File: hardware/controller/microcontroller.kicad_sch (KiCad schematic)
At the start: 43 parts, among them J2 IDC-10, J3 USB_C_Receptacle_USB2.0_14P, SW1 SW_Push, SW2 SW_Push, SW3 SW_Push, U1 STM32U535RET6, U2 nRF24L01+ 2.4Gz Mini SMD, U3 ESP32-C3-WROOM-02, U4 SRV05-4, Y1 8MHz

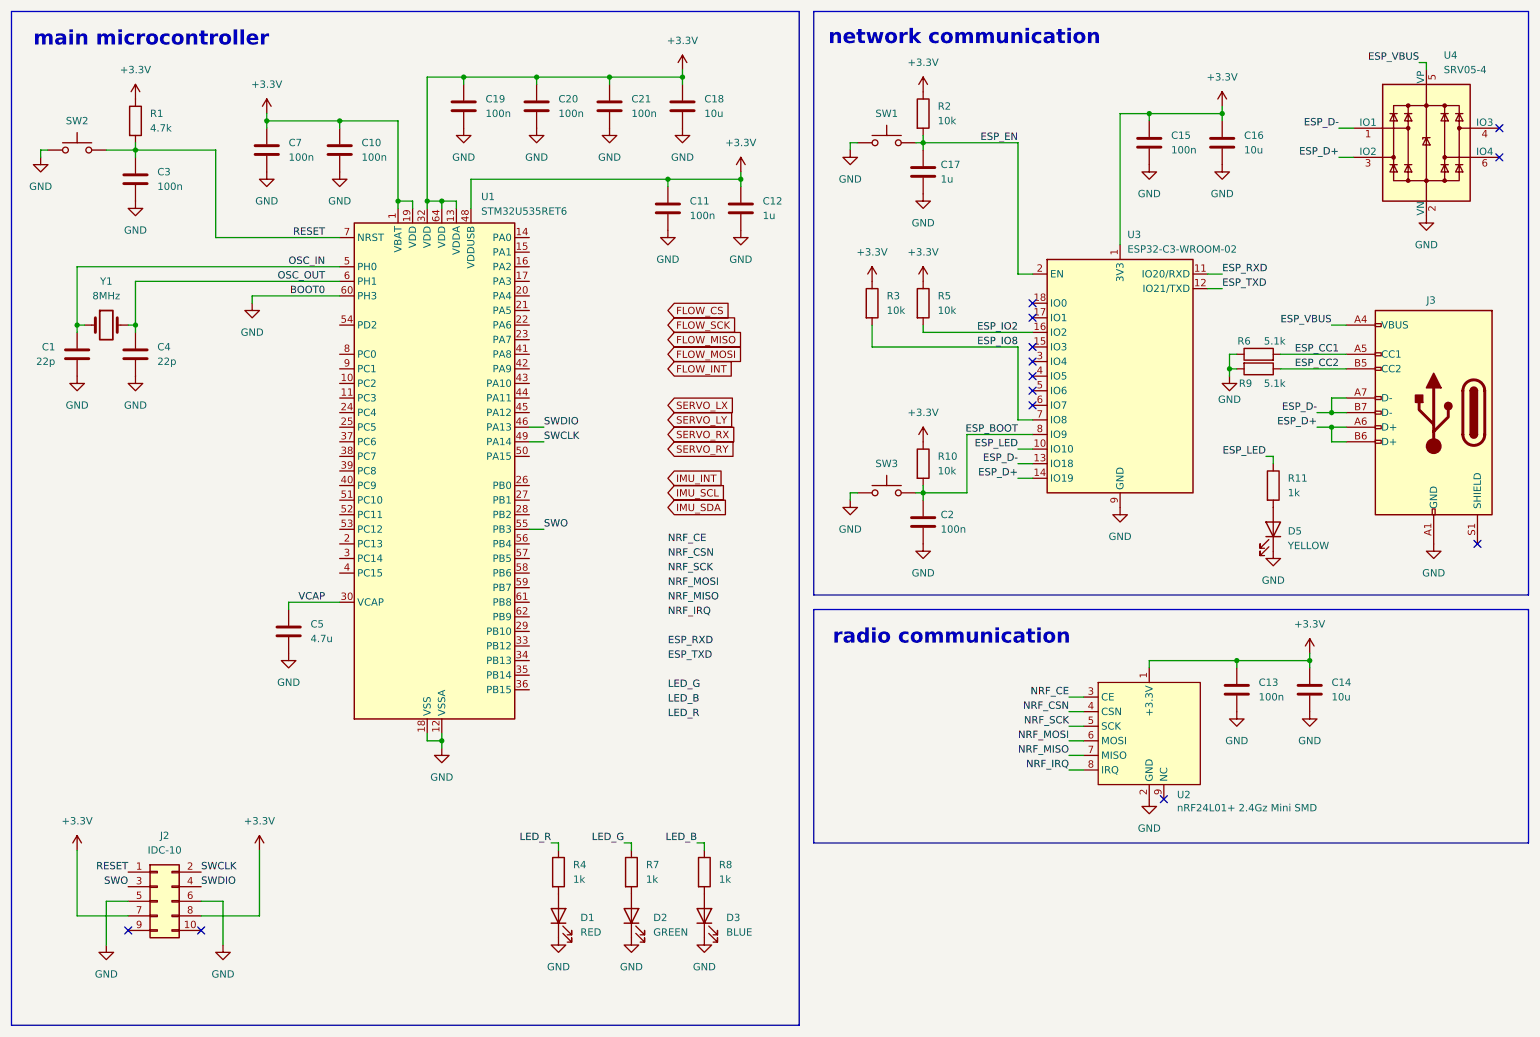
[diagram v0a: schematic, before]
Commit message: add IMU, FLOW, 5V, 3.3V, MOSFET SW
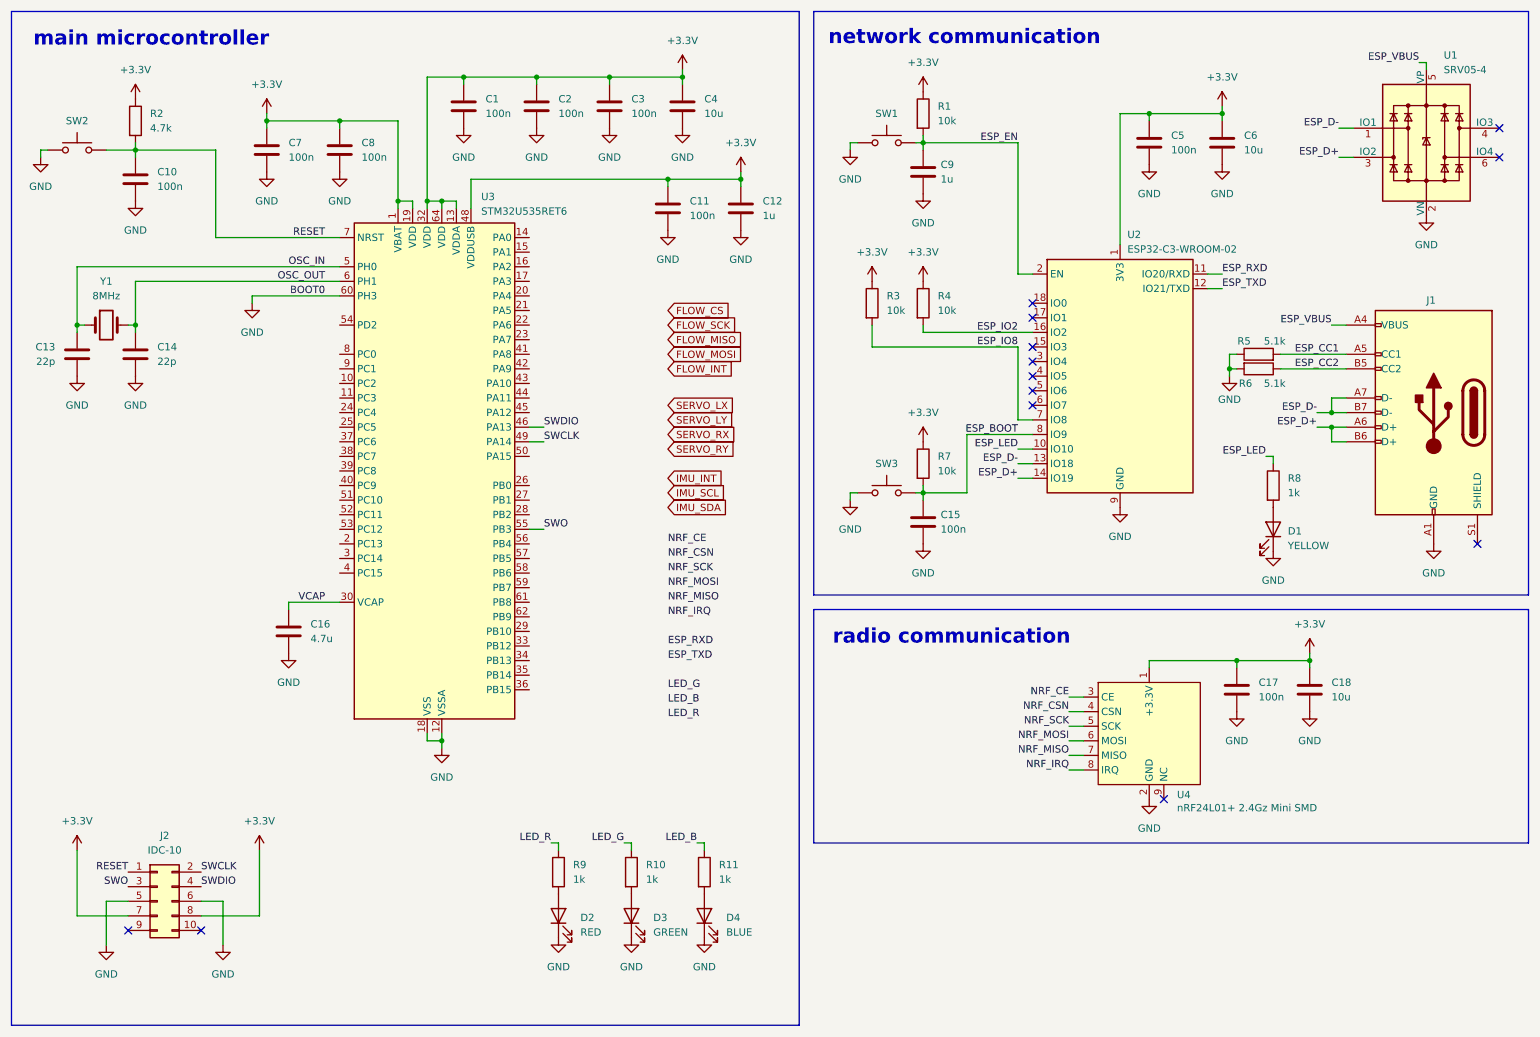
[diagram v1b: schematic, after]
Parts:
- renumbered C19 to C1, C3 to C10, C1 to C13, C4 to C14, C2 to C15, C5 to C16, C13 to C17, C14 to C18, C20 to C2, C21 to C3, C18 to C4, C15 to C5, C16 to C6, C10 to C8, C17 to C9, D5 to D1, D1 to D2, D2 to D3, D3 to D4, J3 to J1, R2 to R1, R7 to R10, R8 to R11, R1 to R2, R5 to R4, R6 to R5, R9 to R6, R10 to R7, R11 to R8, R4 to R9, U4 to U1, U3 to U2, U1 to U3, U2 to U4

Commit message: uC pinout and second power stage
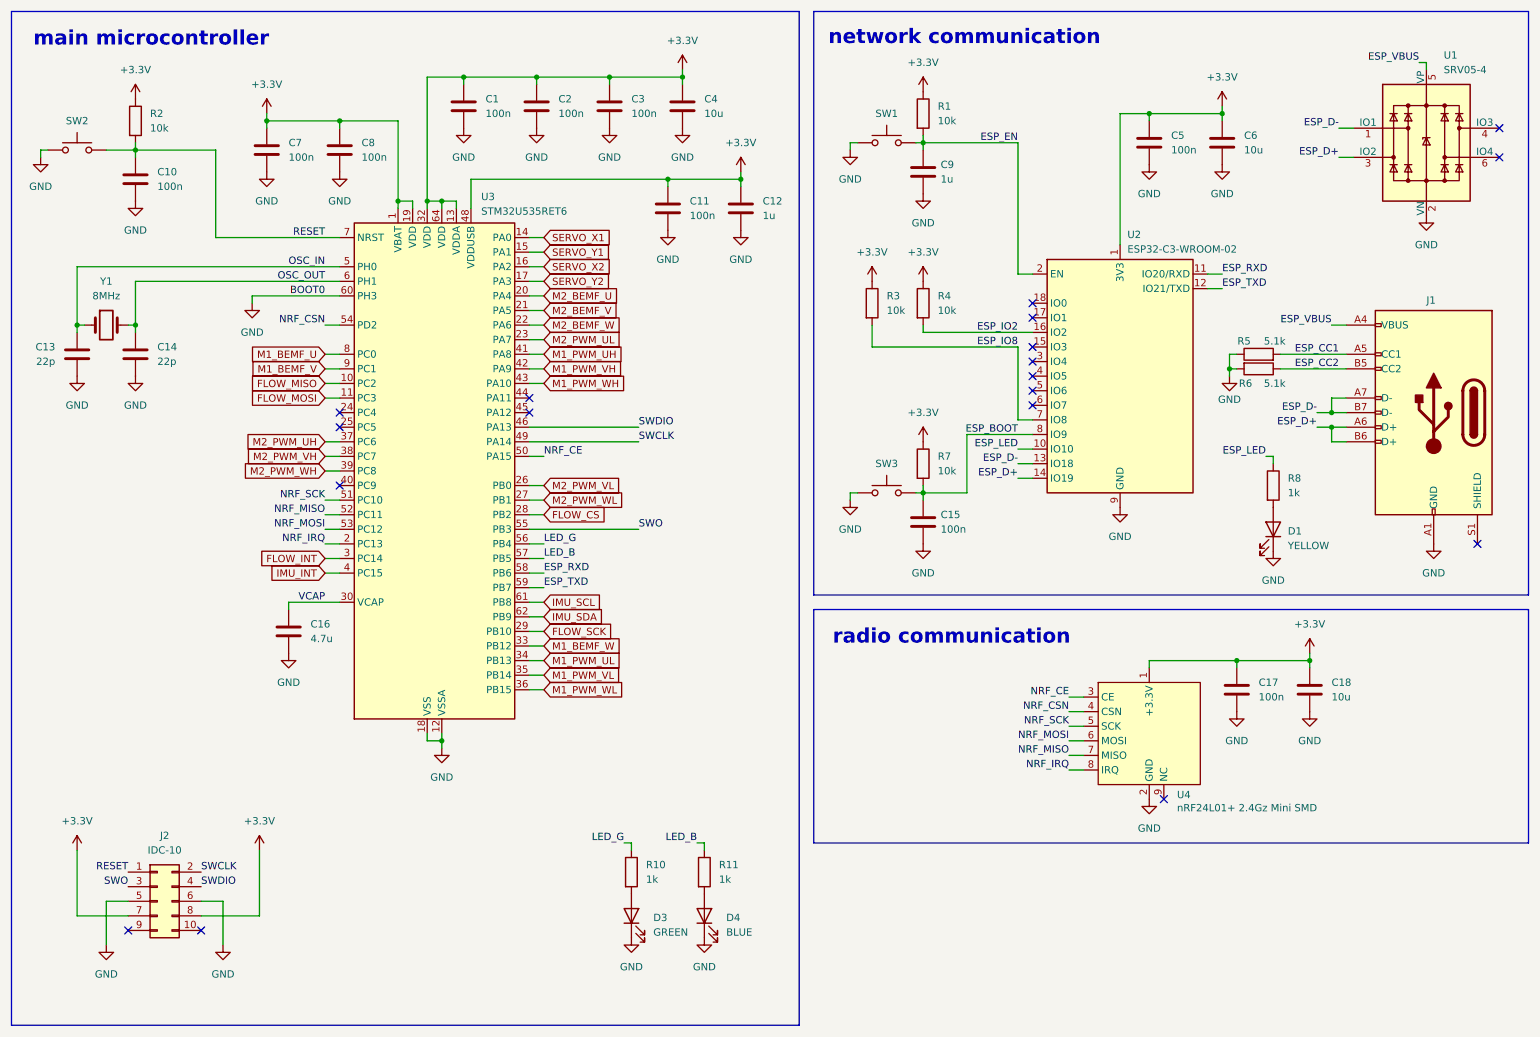
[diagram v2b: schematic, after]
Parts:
- removed D2: RED, LED_SMD:LED_0603_1608Metric, symbol Device:LED
- removed R9: 1k, Resistor_SMD:R_0603_1608Metric, symbol Device:R
- R2: value 4.7k -> 10k
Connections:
- net ESP_RXD: now also U3.58 (PB6)
- net ESP_TXD: now also U3.59 (PB7)
- net FLOW_CS: now also U3.28 (PB2)
- net FLOW_INT: now also U3.3 (PC14)
- net FLOW_MISO: now also U3.10 (PC2)
- net FLOW_MOSI: now also U3.11 (PC3)
- net FLOW_SCK: now also U3.29 (PB10)
- net IMU_INT: now also U3.4 (PC15)
- net IMU_SCL: now also U3.61 (PB8)
- net IMU_SDA: now also U3.62 (PB9)
- net LED_B: now also U3.57 (PB5)
- net LED_G: now also U3.56 (PB4)
- net NRF_CE: now also U3.50 (PA15)
- net NRF_CSN: now also U3.54 (PD2)
- net NRF_IRQ: now also U3.2 (PC13)
- net NRF_MISO: now also U3.52 (PC11)
- net NRF_MOSI: now also U3.53 (PC12)
- net NRF_SCK: now also U3.51 (PC10)
- net SERVO_X1: now reaches U3.14 (PA0)
- net SERVO_Y1: now reaches U3.15 (PA1)
- net SERVO_X2: now reaches U3.16 (PA2)
- net SERVO_Y2: now reaches U3.17 (PA3)
- net M2_BEMF_U: now reaches U3.20 (PA4)
- net M2_BEMF_V: now reaches U3.21 (PA5)
- net M2_BEMF_W: now reaches U3.22 (PA6)
- net M2_PWM_UL: now reaches U3.23 (PA7)
- net M2_PWM_VL: now reaches U3.26 (PB0)
- net M2_PWM_WL: now reaches U3.27 (PB1)
- net M1_BEMF_W: now reaches U3.33 (PB12)
- net M1_PWM_UL: now reaches U3.34 (PB13)
- net M1_PWM_VL: now reaches U3.35 (PB14)
- net M1_PWM_WL: now reaches U3.36 (PB15)
- net M2_PWM_UH: now reaches U3.37 (PC6)
- net M2_PWM_VH: now reaches U3.38 (PC7)
- net M2_PWM_WH: now reaches U3.39 (PC8)
- net M1_PWM_UH: now reaches U3.41 (PA8)
- net M1_PWM_VH: now reaches U3.42 (PA9)
- net M1_PWM_WH: now reaches U3.43 (PA10)
- net M1_BEMF_U: now reaches U3.8 (PC0)
- net M1_BEMF_V: now reaches U3.9 (PC1)
- no-connect marks 13 -> 18
